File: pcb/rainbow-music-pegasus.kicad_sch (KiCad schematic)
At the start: 108 parts, among them J1 USB_B_Micro, J2 Conn_02x03_Odd_Even, J3 B2B-PH-K-S, Q1 DMG3415U, SW1 SW_SPDT, SW2 EVQQ2, U1 ESP32-C3-MINI-1, U2 OPA2322, U3 TLV75533PDBV, U4 MCP73831-2-OT, U5 MCP41050

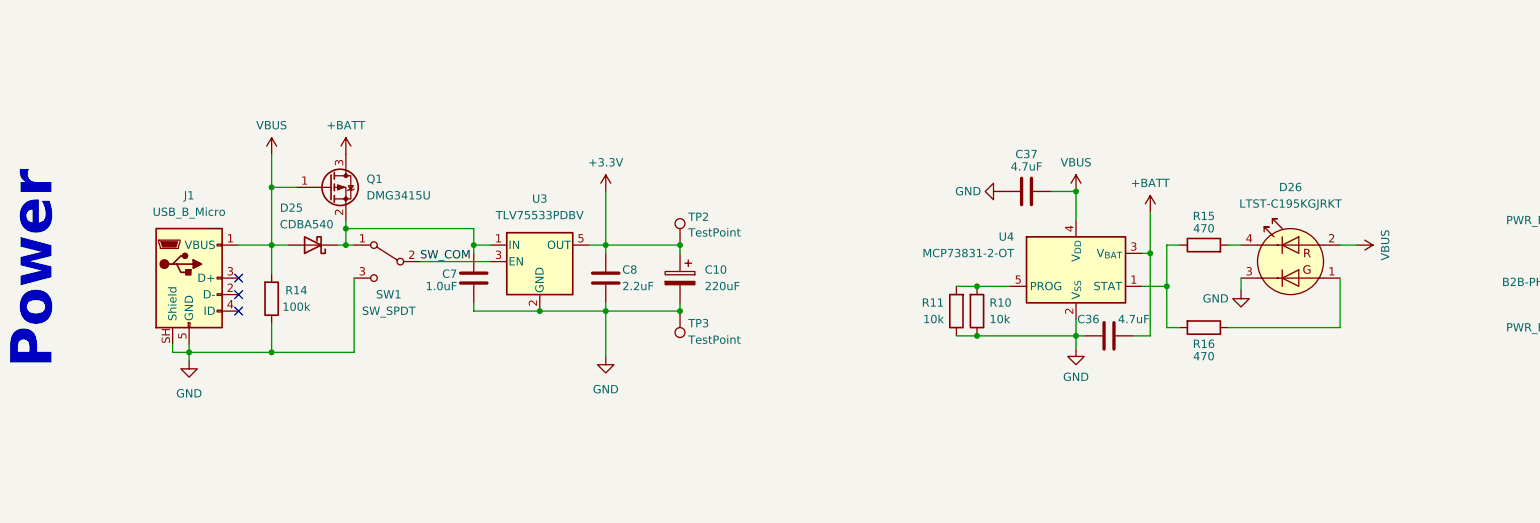
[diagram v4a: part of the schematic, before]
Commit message: Converted the power connector from USB-Mini to USB-C
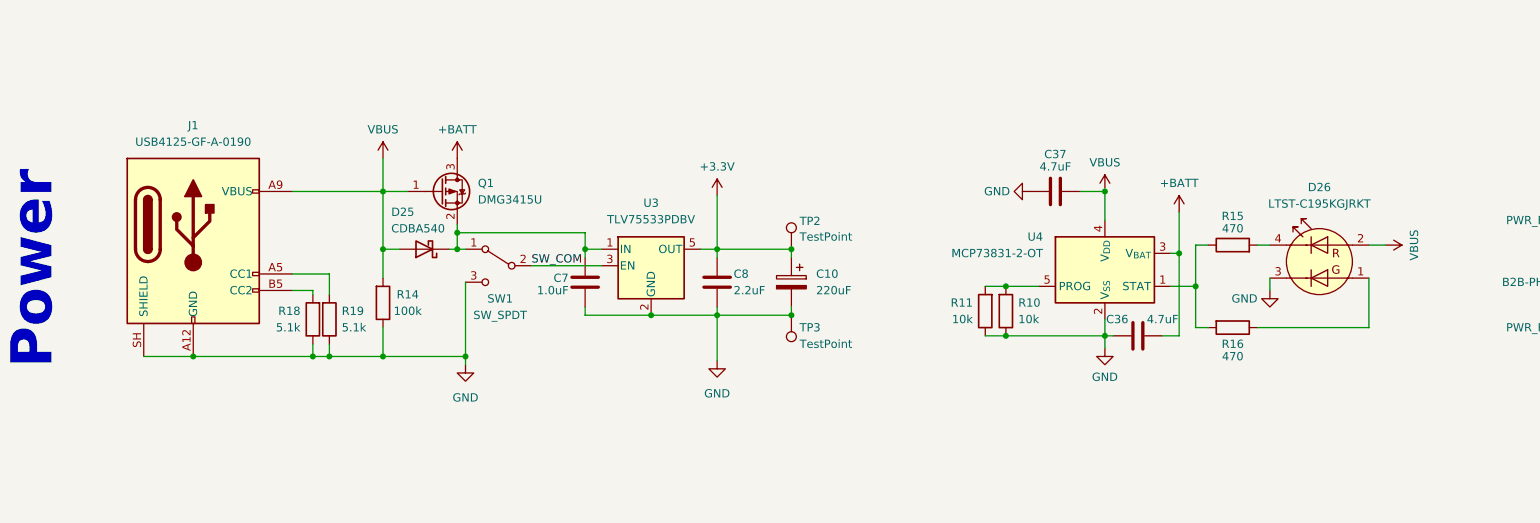
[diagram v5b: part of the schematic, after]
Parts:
- removed J1: USB_B_Micro, Connector_USB:USB_Micro-B_Molex-105017-0001, symbol Connector:USB_B_Micro
- added J1: USB4125-GF-A-0190, Connector_USB:USB_C_Receptacle_HRO_TYPE-C-31-M-17, symbol Connector:USB_C_Receptacle_PowerOnly_6P
- added R18, R19: 5.1k, Resistor_SMD:R_0603_1608Metric, symbol Device:R
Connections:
- net GND: now also J1.A12 (GND), J1.B12 (GND), J1.SH (SHIELD), R18.1, R19.1
- net VBUS: now also J1.A9 (VBUS), J1.B9 (VBUS)
- new net: J1.B5 (CC2), R18.2
- new net: J1.A5 (CC1), R19.2
- no-connect marks 5 -> 2
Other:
- moved on the sheet: C10, C36, C37, C7, C8, D25, D26, Q1, R10, R11, R14, R15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

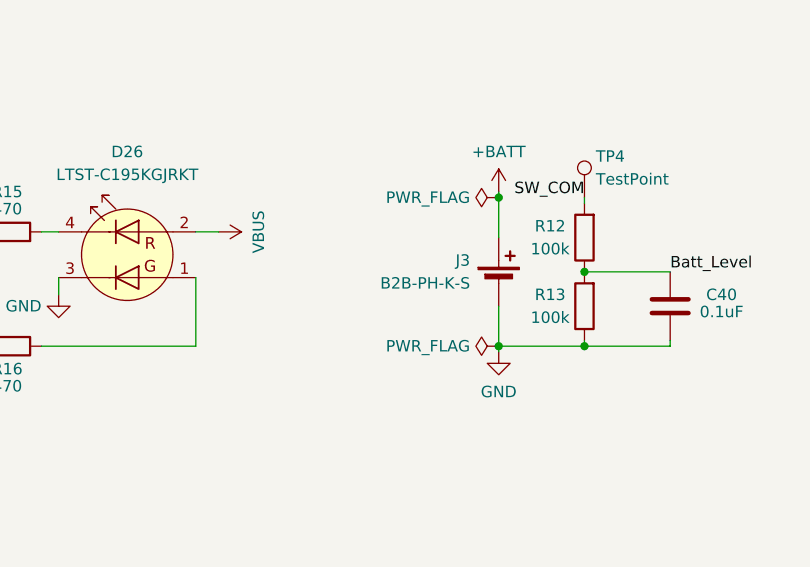
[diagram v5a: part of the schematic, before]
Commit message: Convert the battery connector to a flat-mounted SB2-PH-K-S JST connector
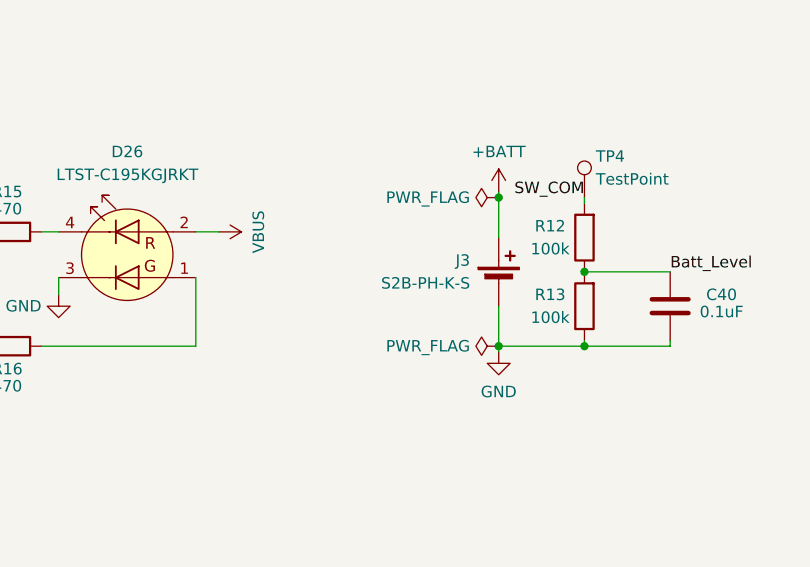
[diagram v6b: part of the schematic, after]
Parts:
- J3: value B2B-PH-K-S -> S2B-PH-K-S; footprint Connector_JST:JST_PH_B2B-PH-K_1x02_P2.00mm_Vertical -> Connector_JST:JST_PH_S2B-PH-K_1x02_P2.00mm_Horizontal
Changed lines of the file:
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@@
 			)
 		)
-		(property "Value" "B2B-PH-K-S"
+		(property "Value" "S2B-PH-K-S"
 			(at 260.985 154.94 0)
 			(show_name no)
@@
 			)
 		)
-		(property "Footprint" "Connector_JST:JST_PH_B2B-PH-K_1x02_P2.00mm_Vertical"
+		(property "Footprint" "Connector_JST:JST_PH_S2B-PH-K_1x02_P2.00mm_Horizontal"
 			(at 264.16 153.416 90)
 			(hide yes)

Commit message: Fixed the J1 footprint to match the USB-C part USB4125-GF-A-0190
Also added a minor overprinting of solder paste to the USB-C mount posts
to better adhere to the board.
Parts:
- J1: footprint Connector_USB:USB_C_Receptacle_HRO_TYPE-C-31-M-17 -> Altivo:USB_C_Receptacle_GCT_USB4125-xx-x-0190_6P_TopMnt_Horizontal
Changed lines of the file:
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@@
 			)
 		)
-		(property "Footprint" "Connector_USB:USB_C_Receptacle_HRO_TYPE-C-31-M-17"
+		(property "Footprint" "Altivo:USB_C_Receptacle_GCT_USB4125-xx-x-0190_6P_TopMnt_Horizontal"
 			(at 53.34 146.05 0)
 			(hide yes)
